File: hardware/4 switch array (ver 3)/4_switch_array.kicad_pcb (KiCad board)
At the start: 2 copper layers, 45.5 x 48.5 mm, 23 parts, among them J1 Conn_01x04, J2 Conn_01x04, J3 Conn_01x02, J4 Conn_01x02, J5 Conn_01x02, J6 Conn_01x02, J7 Conn_01x02, Q1 Q_NPN_EBC, Q2 Q_NPN_EBC, Q3 Q_NPN_EBC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

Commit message: update v3 4 switch array
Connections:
- J1 pad 1: +5V -> SER_IN
- J1 pad 2: GND -> RCLK
- J1 pad 3: SER_IN -> +5V
- J1 pad 4: RCLK -> GND
- J2 pad 1: Net-(J2-Pad1) -> SRCLK
- J2 pad 2: GND -> SRCLR
- J2 pad 3: SRCLK -> Net-(J2-Pad3)
- J2 pad 4: SRCLR -> GND
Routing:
- net +5V: track 13.2 -> 26.7 mm
- net SER_IN: track 9.74 -> 14.8 mm
- net RCLK: track 10.8 -> 13.3 mm
- net SRCLK: track 10.7 -> 9.17 mm
- net SRCLR: track 10.6 -> 9.19 mm

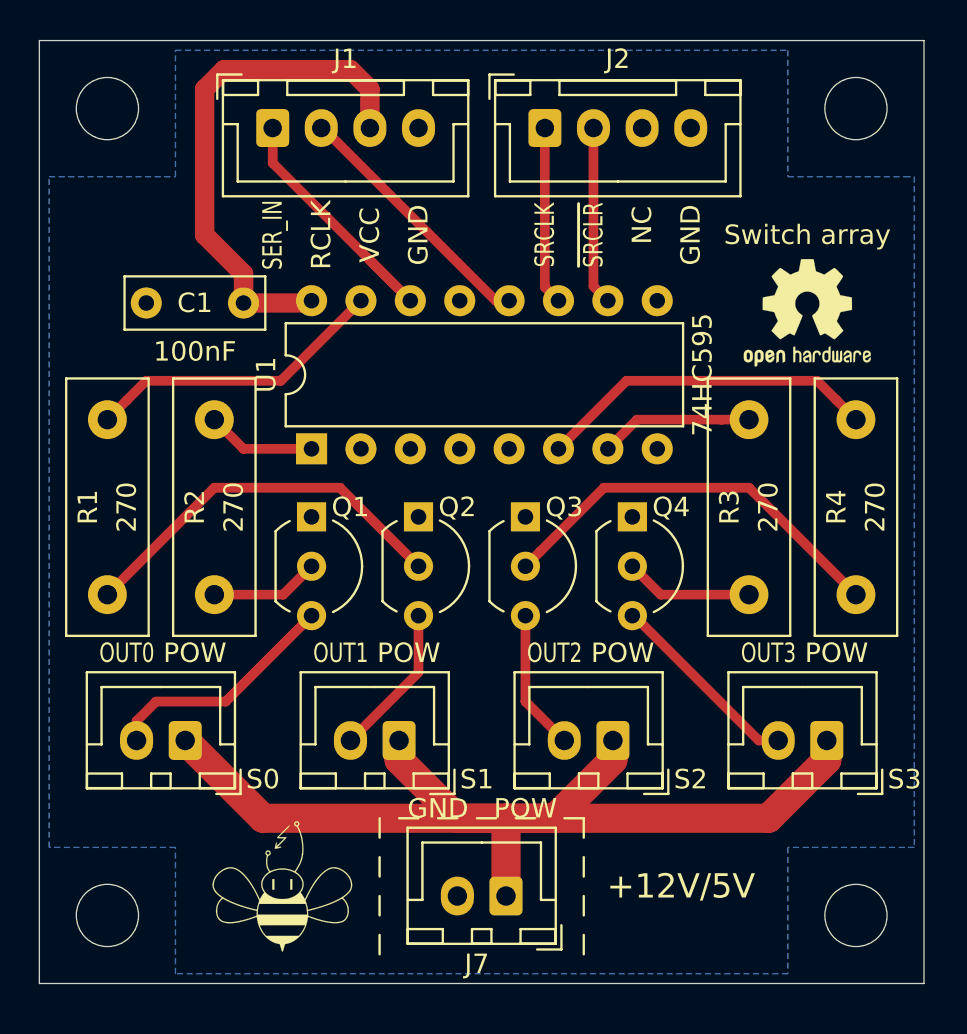
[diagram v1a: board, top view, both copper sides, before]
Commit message: Update on 12V5A system power line
- 12V5A power line is now represented by two connectors with 2 pins across all the modules
- all .png previews are updated. The central hub now has previews for schematics, PCB tracing and 3D model
- peltier module now has two 12V5A connectors with redesigned one side of the bridge. Now all MOSFETs can be equipped with heatsinks
- hum/temp sensor now has its connector position reversed to mimic Grove's one
- hum/temp and gas sensors now have a small BeeHive logo on front layer rather than one big on back layer
- hum/temp sensor now use only one layer for signals and one layer for ground
- switch arrays now have two connectors for 12V5A and 5V3A power lines
- switch arrays had their power lines better traced (no sharp turns)
- power supply (12V5A to 5V3A) now has two connectors for 12V5A power line
- one trace of power supply, which lies in between LM2596's legs, was narrowed to ensure that it will not be accidentally soldered or damaged during placement
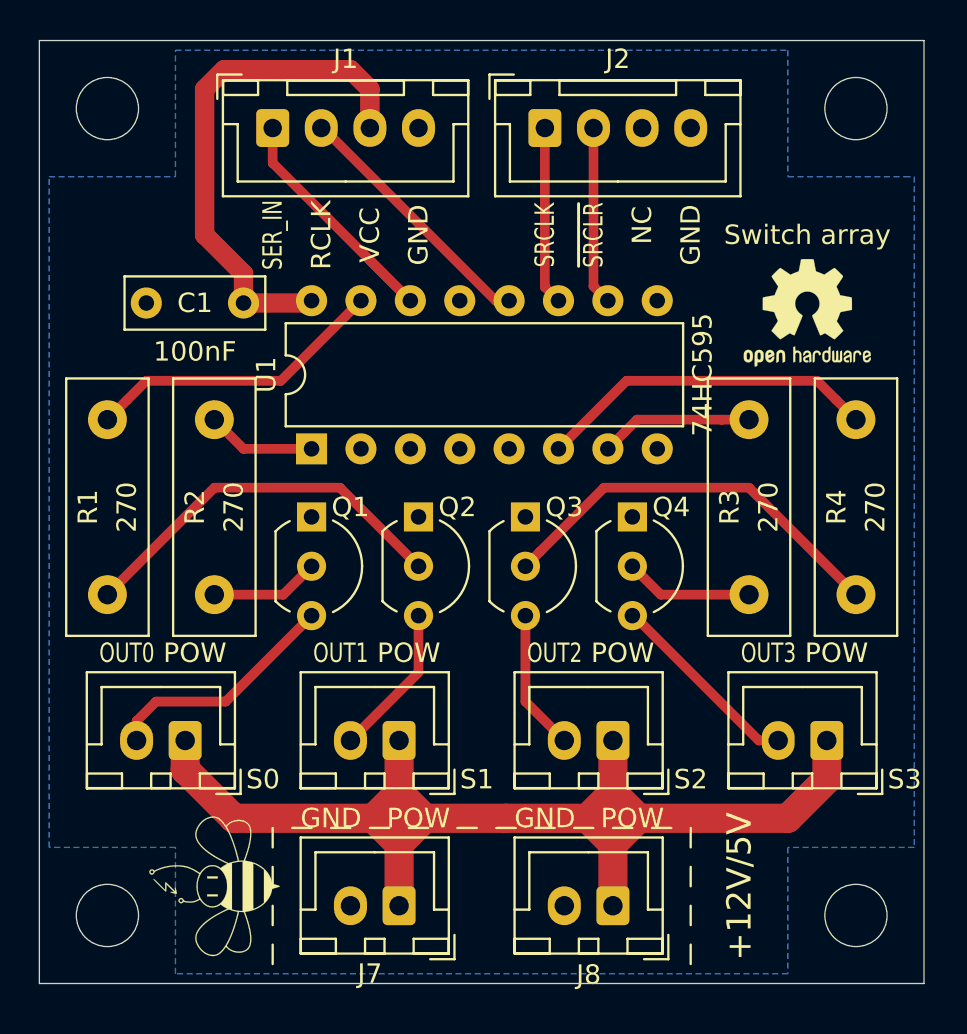
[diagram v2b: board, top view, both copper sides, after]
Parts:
- added J8: Conn_01x02, Connector_JST:JST_XH_B2B-XH-A_1x02_P2.50mm_Vertical, F.Cu at (153.5, 78.0)
- moved J7 5.52 mm to (142.5, 78.0)
- moved G*** 3.50 mm to (133.0, 77.0), turned to 90 degrees
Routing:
- net +12V: track 56.4 -> 72.3 mm
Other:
- rule pad_to_mask_clearance: 0.051 -> 0
